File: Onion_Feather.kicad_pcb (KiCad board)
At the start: 4 copper layers, 59.7 x 53.3 mm, 63 parts, among them IC1 MAX11646EUA+T, J1 HR911105A, J2 CON_HEADER_PRG_AVR_ICSP-PTH, J3 Conn_01x02, J4 USB_A, J5 M04PTH, U1 ONION-OMEGA2, U2 AP1117-33, U3 CP2102N-A01-GQFN24, U4 BQ25895RTW, U5 STF202-22T1G

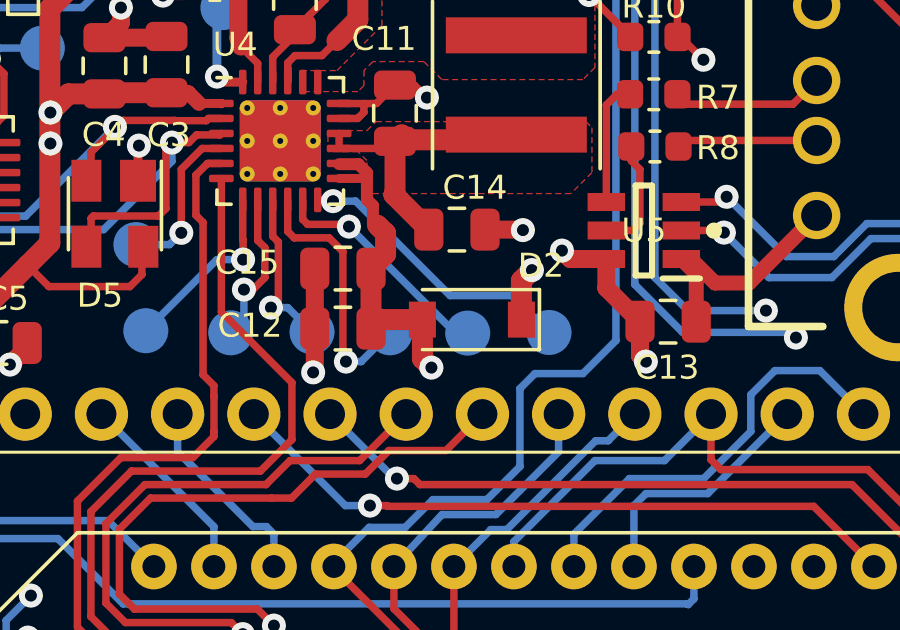
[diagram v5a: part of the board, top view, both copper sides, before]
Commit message: WIP on diode OR
Signed-off-by: Tisham Dhar <whatnickd@gmail.com>
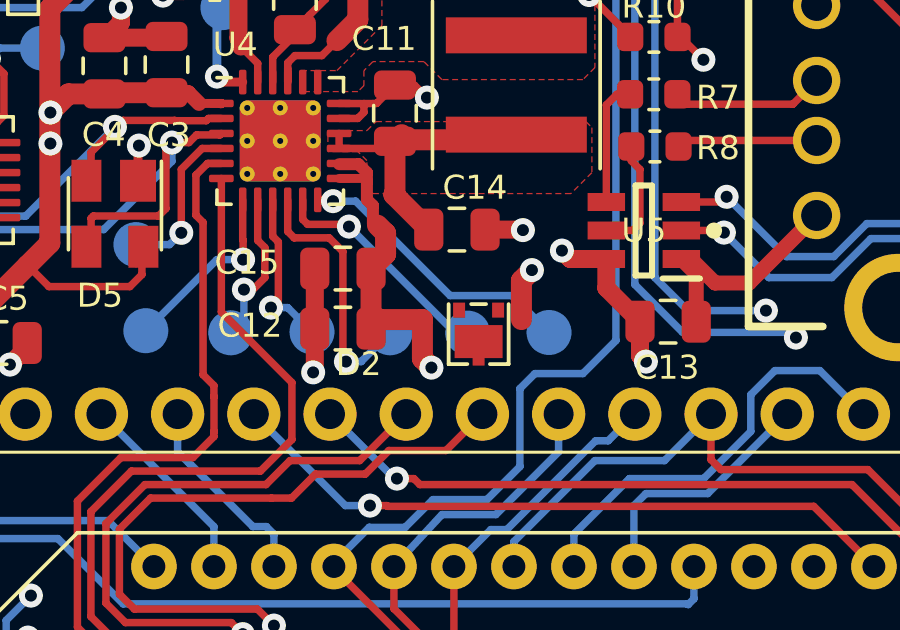
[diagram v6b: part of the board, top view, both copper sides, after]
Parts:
- D2: value MBR130T3G -> D_Schottky_x2_KCom_AAK; footprint Diode_SMD:D_SOD-123 -> footprints:SOT1061
- moved D2 0.53 mm to (145.9, 79.9)
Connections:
- U2 pad 3: VIN -> Net-(D2-Pad3)
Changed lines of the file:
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@@
     (zones 0)
     (modules 63)
-    (nets 82)
+    (nets 83)
   )
   (page A4)
@@
   (net 80 "Net-(U3-Pad9)")
   (net 81 "Net-(U3-Pad1)")
+  (net 82 "Net-(D2-Pad3)")
   (net_class Default "This is the default net class."
     (clearance 0.2)
@@
     (add_net "Net-(C7-Pad1)")
     (add_net "Net-(C7-Pad2)")
+    (add_net "Net-(D2-Pad3)")
     (add_net "Net-(IC1-Pad3)")
     (add_net "Net-(J1-Pad10)")
@@
     (add_net VIN)
     (add_net ~RESET)
+  )
+  (module footprints:SOT1061 (layer F.Cu)
+    (at 145.923 79.883 180)
+    (descr "<li><b>SOT1061</b><hr> <ul><li>HUSON3: plastic thermal enhanced ultra thin small outline package; no leads;3 terminals; body 2 x 2 x 0.65 mm<li><u>JEDEC</u>: -- <li><u>IEC</u>: -- <li><u>JEITA</u>: --</ul>")
+    (fp_text reference D2 (at 4 -1) (layer F.SilkS)
+      (effects (font (size 0.787402 0.787402) (thickness 0.015)))
+    )
+    (fp_text value D_Schottky_x2_KCom_AAK (at 5 0.5) (layer F.Fab)
+      (effects (font (size 0.787402 0.787402) (thickness 0.015)))
+    )
+    (fp_poly (pts (xy 0.85 0.35) (xy -0.85 0.35) (xy -0.85 -0.85) (xy -0.25 -0.85)
+      (xy -0.25 -1.1) (xy 0.25 -1.1) (xy 0.25 -0.85) (xy 0.85 -0.85)) (layer F.Mask) (width 0))
+    (fp_poly (pts (xy 0.8 0.3) (xy -0.8 0.3) (xy -0.8 -0.8) (xy -0.2 -0.8)
+      (xy -0.2 -1.05) (xy 0.2 -1.05) (xy 0.2 -0.8) (xy 0.8 -0.8)) (layer F.Cu) (width 0))
+    (fp_poly (pts (xy 0.8 0.3) (xy -0.8 0.3) (xy -0.8 -0.8) (xy -0.2 -0.8)
+      (xy -0.2 -1.05) (xy 0.2 -1.05) (xy 0.2 -0.8) (xy 0.8 -0.8)) (layer F.Paste) (width 0))
+    (fp_poly (pts (xy -1 0) (xy 0 0) (xy 0 1) (xy -1 1)) (layer F.Fab) (width 0.01))
+    (fp_poly (pts (xy 0.4 0.5) (xy 0.9 0.5) (xy 0.9 1.1) (xy 0.4 1.1)) (layer F.Mask) (width 0.01))
+    (fp_poly (pts (xy -0.9 0.5) (xy -0.4 0.5) (xy -0.4 1.1) (xy -0.9 1.1)) (layer F.Mask) (width 0.01))
+    (fp_line (start 0.25 1) (end -0.25 1) (layer F.SilkS) (width 0.125))
+    (fp_line (start -1 -1) (end -1 1) (layer F.SilkS) (width 0.125))
+    (fp_line (start -0.375 -1) (end -1 -1) (layer F.SilkS) (width 0.125))
+    (fp_line (start 1 -1) (end 0.375 -1) (layer F.SilkS) (width 0.125))
+    (fp_line (start 1 1) (end 1 -1) (layer F.SilkS) (width 0.125))
+    (fp_line (start 1 -0.9) (end 1 1) (layer F.Fab) (width 0.125))
+    (fp_line (start 1 -1) (end 1 -0.9) (layer F.Fab) (width 0.125))
+    (fp_line (start -1 -1) (end 1 -1) (layer F.Fab) (width 0.125))
+    (fp_line (start -1 1) (end -1 -1) (layer F.Fab) (width 0.125))
+    (fp_line (start 1 1) (end -1 1) (layer F.Fab) (width 0.125))
+    (pad 3 smd rect (at 0 -0.875 180) (size 0 0) (layers F.Cu)
+      (net 82 "Net-(D2-Pad3)"))
+    (pad 2 smd rect (at 0.65 0.8 180) (size 0.4 0.5) (layers F.Cu F.Paste)
+      (net 21 VBAT))
+    (pad 1 smd rect (at -0.65 0.8 180) (size 0.4 0.5) (layers F.Cu F.Paste)
+      (net 2 VIN))
   )
   (module Resistor_SMD:R_0603_1608Metric (layer F.Cu)
@@
       (net 1 GND))
     (pad 3 smd rect (at -3.15 2.3 90) (size 2 1.5) (layers F.Cu F.Paste F.Mask)
-      (net 2 VIN))
+      (net 82 "Net-(D2-Pad3)"))
     (pad 2 smd rect (at -3.15 0 90) (size 2 1.5) (layers F.Cu F.Paste F.Mask)
       (net 3 3.3V))
@@
       (net 58 "/Power Subsystems/ID"))
   )
-  (module Diode_SMD:D_SOD-123 (layer F.Cu)
-    (at 145.7 79.4 180)
-    (descr SOD-123)
-    (tags SOD-123)
-    (attr smd)
-    (fp_text reference D2 (at -2.3 1.8) (layer F.SilkS)
-      (effects (font (size 0.8 0.8) (thickness 0.2)))
-    )
-    (fp_text value MBR130T3G (at 0 2.1) (layer F.Fab)
-      (effects (font (size 1 1) (thickness 0.15)))
-    )
-    (fp_text user %R (at 0 -2) (layer F.Fab)
-      (effects (font (size 0.8 0.8) (thickness 0.2)))
-    )
-    (fp_line (start -2.25 -1) (end -2.25 1) (layer F.SilkS) (width 0.12))
-    (fp_line (start 0.25 0) (end 0.75 0) (layer F.Fab) (width 0.1))
-    (fp_line (start 0.25 0.4) (end -0.35 0) (layer F.Fab) (width 0.1))
-    (fp_line (start 0.25 -0.4) (end 0.25 0.4) (layer F.Fab) (width 0.1))
-    (fp_line (start -0.35 0) (end 0.25 -0.4) (layer F.Fab) (width 0.1))
-    (fp_line (start -0.35 0) (end -0.35 0.55) (layer F.Fab) (width 0.1))
-    (fp_line (start -0.35 0) (end -0.35 -0.55) (layer F.Fab) (width 0.1))
-    (fp_line (start -0.75 0) (end -0.35 0) (layer F.Fab) (width 0.1))
-    (fp_line (start -1.4 0.9) (end -1.4 -0.9) (layer F.Fab) (width 0.1))
-    (fp_line (start 1.4 0.9) (end -1.4 0.9) (layer F.Fab) (width 0.1))
-    (fp_line (start 1.4 -0.9) (end 1.4 0.9) (layer F.Fab) (width 0.1))
-    (fp_line (start -1.4 -0.9) (end 1.4 -0.9) (layer F.Fab) (width 0.1))
-    (fp_line (start -2.35 -1.15) (end 2.35 -1.15) (layer F.CrtYd) (width 0.05))
-    (fp_line (start 2.35 -1.15) (end 2.35 1.15) (layer F.CrtYd) (width 0.05))
-    (fp_line (start 2.35 1.15) (end -2.35 1.15) (layer F.CrtYd) (width 0.05))
-    (fp_line (start -2.35 -1.15) (end -2.35 1.15) (layer F.CrtYd) (width 0.05))
-    (fp_line (start -2.25 1) (end 1.65 1) (layer F.SilkS) (width 0.12))
-    (fp_line (start -2.25 -1) (end 1.65 -1) (layer F.SilkS) (width 0.12))
-    (pad 1 smd rect (at -1.65 0 180) (size 0.9 1.2) (layers F.Cu F.Paste F.Mask)
-      (net 2 VIN))
-    (pad 2 smd rect (at 1.65 0 180) (size 0.9 1.2) (layers F.Cu F.Paste F.Mask)
-      (net 21 VBAT))
-    (model ${KISYS3DMOD}/Diode_SMD.3dshapes/D_SOD-123.wrl
-      (at (xyz 0 0 0))
-      (scale (xyz 1 1 1))
-      (rotate (xyz 0 0 0))
-    )
-  )
   (gr_text "Onion-Omega to Feather Adapter\nv0.0.1 20/04/2020\nby Tisham (whatnick) Dhar\nOSHW TAPR" (at 149.86 95.25) (layer B.SilkS)

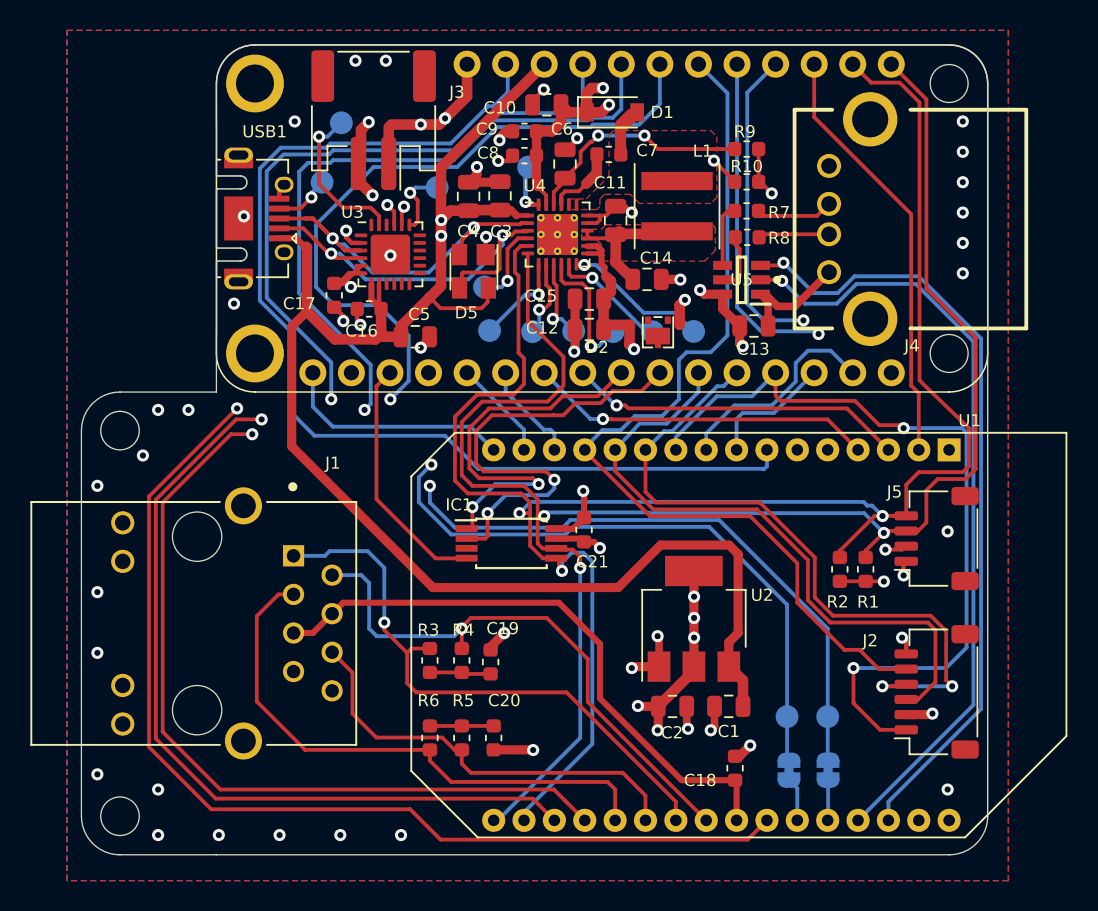
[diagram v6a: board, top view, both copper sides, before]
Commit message: Use common cathode and reroute
Signed-off-by: Tisham Dhar <whatnickd@gmail.com>
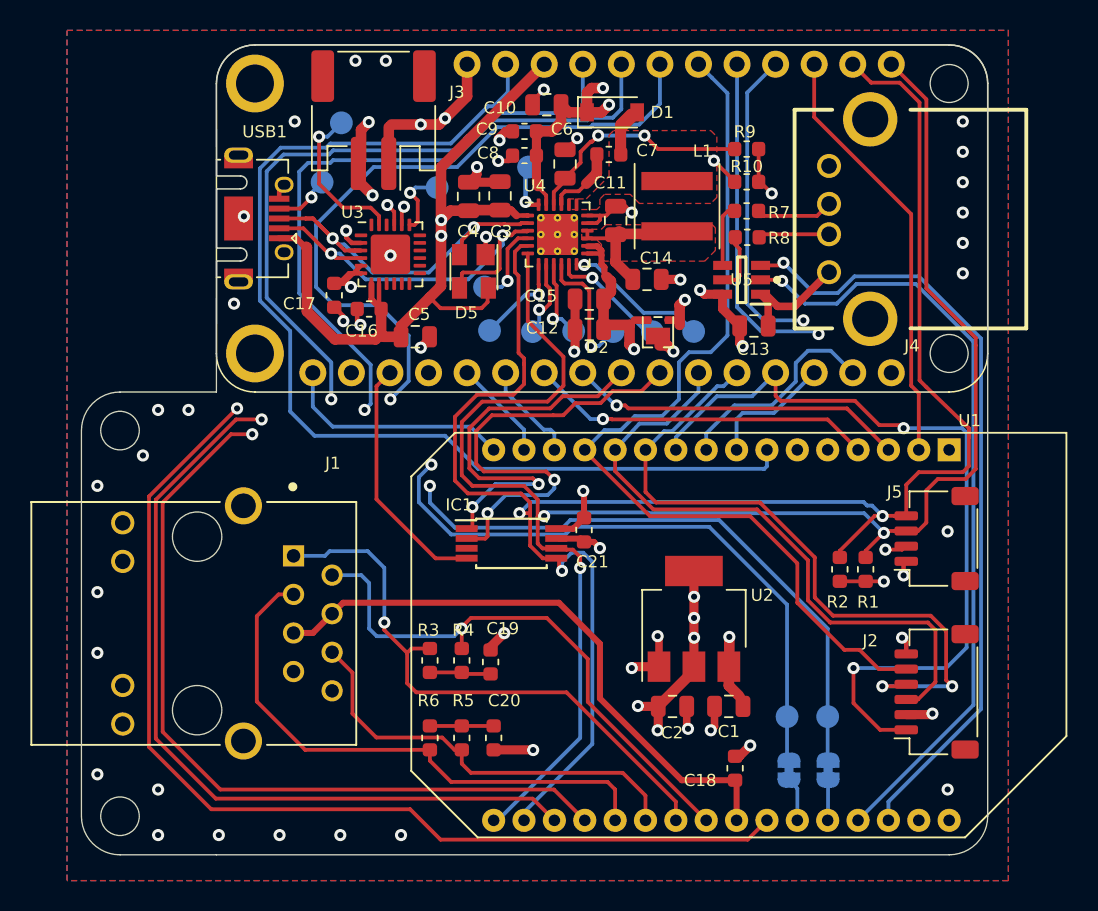
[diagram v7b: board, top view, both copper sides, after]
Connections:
- C1 pad 1: VIN -> /Power Subsystems/V_UPS
- D2 pad 3: Net-(D2-Pad3) -> /Power Subsystems/V_UPS
- U2 pad 3: Net-(D2-Pad3) -> /Power Subsystems/V_UPS
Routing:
- net /Power Subsystems/V_UPS: track 0.00 -> 56.4 mm, vias 0 -> 2
- net VIN: track 129.0 -> 75.3 mm
- net VBAT: track 52.2 -> 53.5 mm

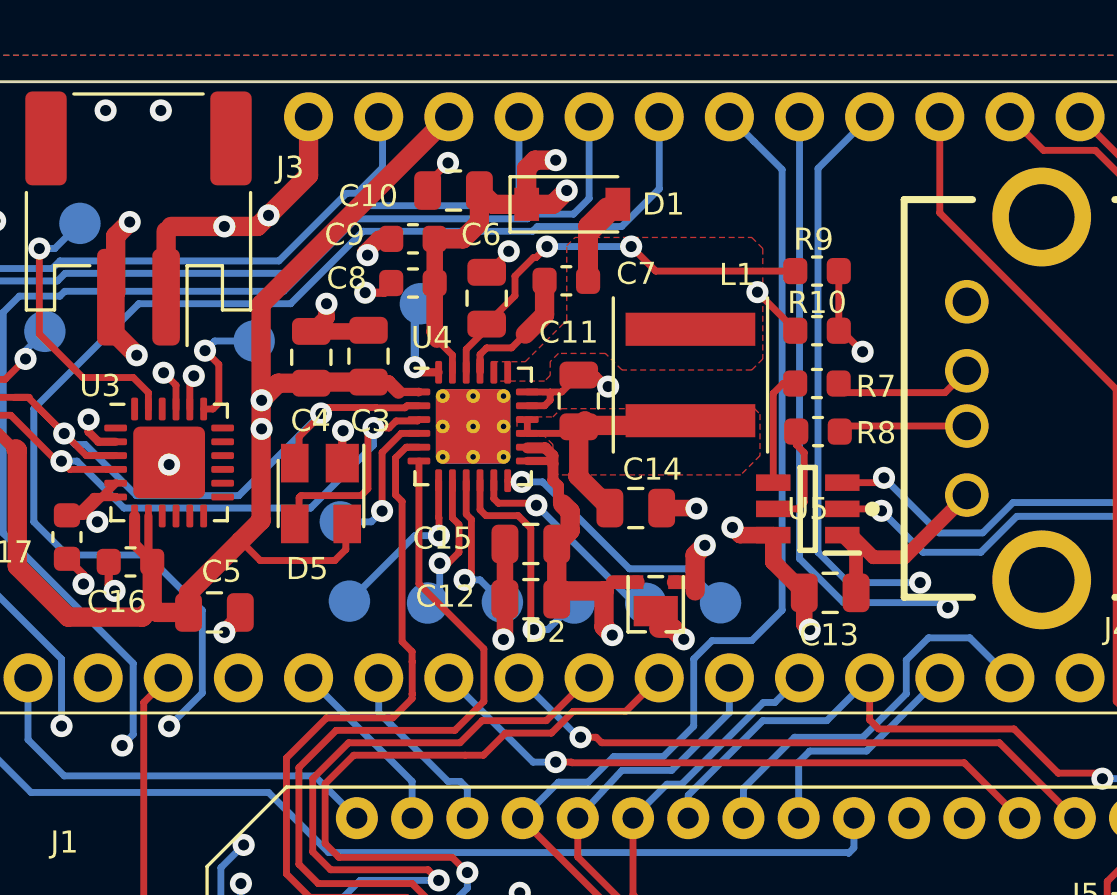
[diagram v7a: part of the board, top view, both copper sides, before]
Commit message: #5 Add OTG bias and clean up courtyard
Signed-off-by: Tisham Dhar <whatnickd@gmail.com>
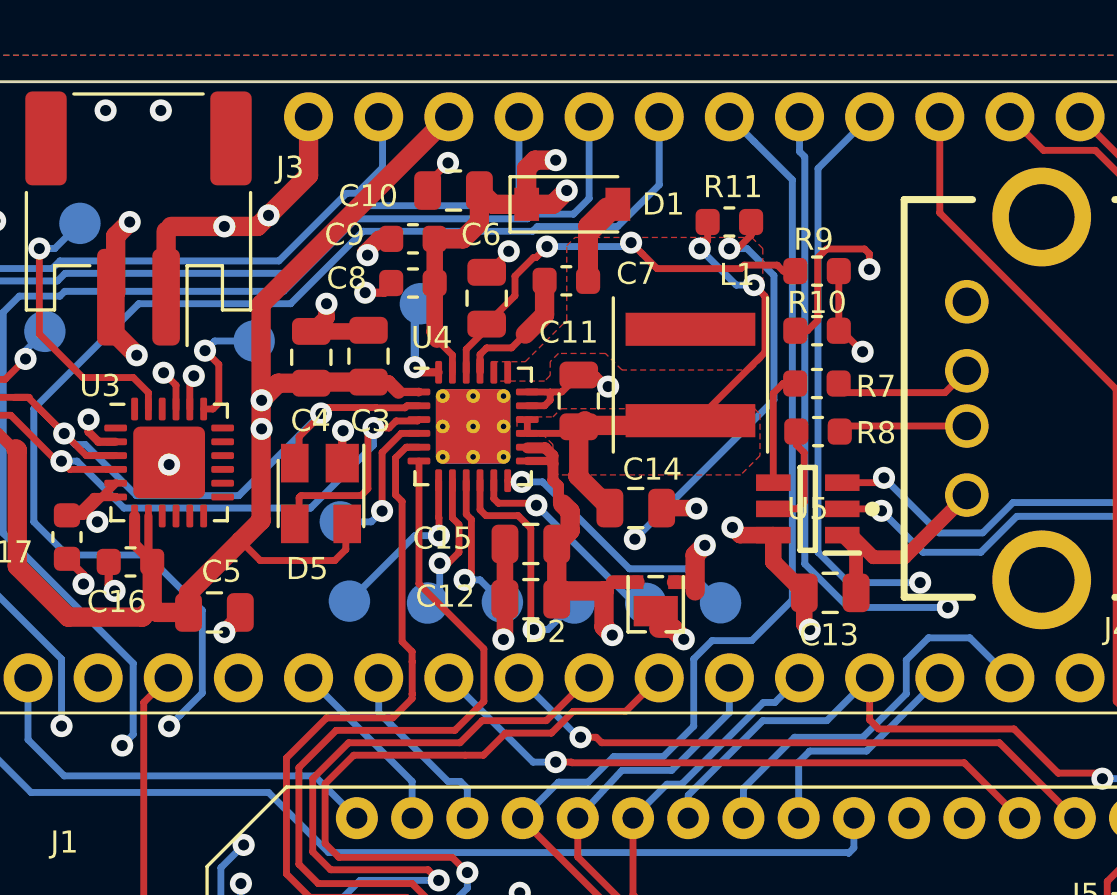
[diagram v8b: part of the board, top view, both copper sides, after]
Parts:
- added R11: 10K, Resistor_SMD:R_0603_1608Metric, F.Cu at (148.6, 66.0)
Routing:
- net /Power Subsystems/OTG: track 5.18 -> 27.7 mm, vias 1 -> 3
- net /Power Subsystems/SYS: track 10.2 -> 20.1 mm, vias 0 -> 2
- net GND: track 55.7 -> 59.6 mm
